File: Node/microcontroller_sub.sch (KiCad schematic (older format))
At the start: 53 parts, among them SW1701 SW_Push, U1701 IC_MICROCHIP_SAMD21G18A-A, Y2301 32.768kHz, Y2302 25MHz

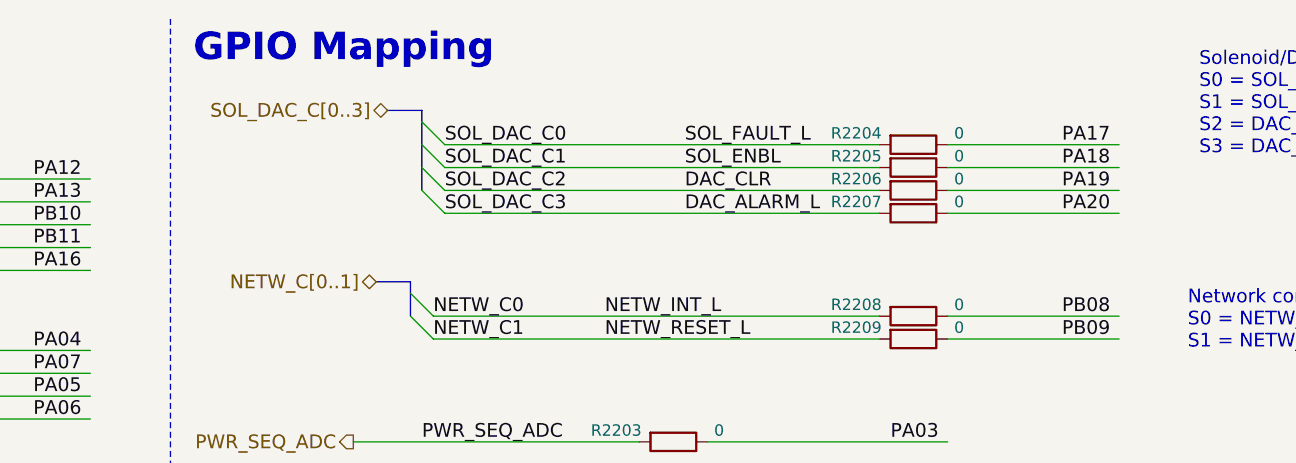
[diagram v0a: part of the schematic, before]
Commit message: All layout done. Added PU to the ADC mux. Assigned SAMD pins to the DAC power sequencer I/O. Cleaned up the power layer. Time for DRC, cleaning, minute tweaks, and documentation/BOM
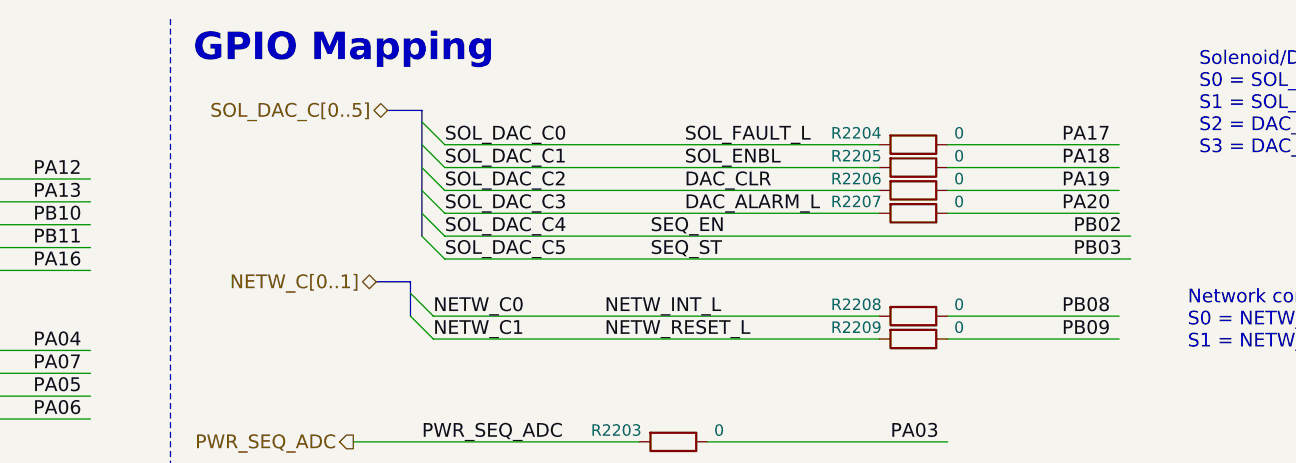
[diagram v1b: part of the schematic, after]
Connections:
- net labels added: SEQ_EN, SEQ_ST, SOL_DAC_C4, SOL_DAC_C5, SOL_DAC_C[0..5]
- net labels removed: SOL_DAC_C[0..3]
- wire segments 161 -> 163
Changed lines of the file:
@@
 I2C Capable Pins:\nSERCOM4: 21+22\nSERCOM3: 25+26\nSERCOM5: 31+32\nSERCOM2: 13+14\n
 $Comp
-L GND #PWR2213
+L GND #PWR2214
 U 1 1 59E6B342
 P 6750 10150
-F 0 "#PWR2213" H 6750 9900 50  0001 C CNN
+F 0 "#PWR2214" H 6750 9900 50  0001 C CNN
 F 1 "GND" H 6750 10000 50  0000 C CNN
 F 2 "" H 6750 10150 50  0000 C CNN
@@
 $EndComp
 $Comp
-L GND #PWR2205
+L GND #PWR2207
 U 1 1 59E72263
 P 1250 4350
-F 0 "#PWR2205" H 1250 4100 50  0001 C CNN
+F 0 "#PWR2207" H 1250 4100 50  0001 C CNN
 F 1 "GND" H 1250 4200 50  0000 C CNN
 F 2 "" H 1250 4350 50  0000 C CNN
@@
 VDDCORE_1V2
 $Comp
-L GND #PWR2211
+L GND #PWR2204
 U 1 1 5A0AA08F
 P 4500 2100
-F 0 "#PWR2211" H 4500 1850 50  0001 C CNN
+F 0 "#PWR2204" H 4500 1850 50  0001 C CNN
 F 1 "GND" H 4500 1950 50  0000 C CNN
 F 2 "" H 4500 2100 50  0001 C CNN
@@
 RESET_L
 $Comp
-L GND #PWR2208
+L GND #PWR2206
 U 1 1 5A0AC21B
 P 2100 4200
-F 0 "#PWR2208" H 2100 3950 50  0001 C CNN
+F 0 "#PWR2206" H 2100 3950 50  0001 C CNN
 F 1 "GND" H 2100 4050 50  0000 C CNN
 F 2 "" H 2100 4200 50  0000 C CNN
@@
 GPIO Mapping
 Text HLabel 11150 900  0    60   BiDi ~ 0
-SOL_DAC_C[0..3]
+SOL_DAC_C[0..5]
 Entry Wire Line
 	11300 950  11400 1050
@@
 $EndComp
 $Comp
-L GND #PWR2210
+L GND #PWR2203
 U 1 1 5A13F166
 P 2800 2000
-F 0 "#PWR2210" H 2800 1750 50  0001 C CNN
+F 0 "#PWR2203" H 2800 1750 50  0001 C CNN
 F 1 "GND" H 2800 1850 50  0000 C CNN
 F 2 "" H 2800 2000 50  0001 C CNN
@@
 $EndComp
 $Comp
-L +3V3 #PWR2202
+L +3V3 #PWR2201
 U 1 1 5A13F196
 P 850 1200
-F 0 "#PWR2202" H 850 1050 50  0001 C CNN
+F 0 "#PWR2201" H 850 1050 50  0001 C CNN
 F 1 "+3V3" H 850 1340 50  0000 C CNN
 F 2 "" H 850 1200 50  0001 C CNN
@@
 $EndComp
 $Comp
-L GND #PWR2203
+L GND #PWR2202
 U 1 1 5A1411D0
 P 850 2000
-F 0 "#PWR2203" H 850 1750 50  0001 C CNN
+F 0 "#PWR2202" H 850 1750 50  0001 C CNN
 F 1 "GND" H 850 1850 50  0000 C CNN
 F 2 "" H 850 2000 50  0001 C CNN
@@
 $EndComp
 $Comp
-L +3V3 #PWR2209
+L +3V3 #PWR2205
 U 1 1 5A1416C8
 P 2700 2800
-F 0 "#PWR2209" H 2700 2650 50  0001 C CNN
+F 0 "#PWR2205" H 2700 2650 50  0001 C CNN
 F 1 "+3V3" H 2700 2940 50  0000 C CNN
 F 2 "" H 2700 2800 50  0001 C CNN
@@
 3V3A_SAMD
 $Comp
-L +3V3 #PWR2212
+L +3V3 #PWR2209
 U 1 1 5A142050
 P 6450 6200
-F 0 "#PWR2212" H 6450 6050 50  0001 C CNN
+F 0 "#PWR2209" H 6450 6050 50  0001 C CNN
 F 1 "+3V3" H 6450 6340 50  0000 C CNN
 F 2 "" H 6450 6200 50  0001 C CNN
@@
 $EndComp
 $Comp
-L +3V3 #PWR2214
+L +3V3 #PWR2208
 U 1 1 5A0D576C
 P 7700 4650
-F 0 "#PWR2214" H 7700 4500 50  0001 C CNN
+F 0 "#PWR2208" H 7700 4500 50  0001 C CNN
 F 1 "+3V3" H 7700 4790 50  0000 C CNN
 F 2 "" H 7700 4650 50  0001 C CNN
@@
 $EndComp
 $Comp
-L GND #PWR2201
+L GND #PWR2210
 U 1 1 5A0DF272
 P 800 6600
-F 0 "#PWR2201" H 800 6350 50  0001 C CNN
+F 0 "#PWR2210" H 800 6350 50  0001 C CNN
 F 1 "GND" H 800 6450 50  0000 C CNN
 F 2 "" H 800 6600 50  0000 C CNN
@@
 $EndComp
 $Comp
-L GND #PWR2206
+L GND #PWR2211
 U 1 1 5A0DF2F9
 P 1600 6600
-F 0 "#PWR2206" H 1600 6350 50  0001 C CNN
+F 0 "#PWR2211" H 1600 6350 50  0001 C CNN
 F 1 "GND" H 1600 6450 50  0000 C CNN
 F 2 "" H 1600 6600 50  0000 C CNN
@@
 $EndComp
 $Comp
-L GND #PWR2204
+L GND #PWR2212
 U 1 1 5A0E3348
 P 850 8900
-F 0 "#PWR2204" H 850 8650 50  0001 C CNN
+F 0 "#PWR2212" H 850 8650 50  0001 C CNN
 F 1 "GND" H 850 8750 50  0000 C CNN
 F 2 "" H 850 8900 50  0000 C CNN
@@
 $EndComp
 $Comp
-L GND #PWR2207
+L GND #PWR2213
 U 1 1 5A0E334F
 P 1650 8900
-F 0 "#PWR2207" H 1650 8650 50  0001 C CNN
+F 0 "#PWR2213" H 1650 8650 50  0001 C CNN
 F 1 "GND" H 1650 8750 50  0000 C CNN
 F 2 "" H 1650 8900 50  0000 C CNN
@@
 	500  4750 3650 4750
 Wire Bus Line
-	11300 900  11300 1250
+	11300 900  11300 1450
 Wire Wire Line
 	11400 1050 13300 1050
@@
 Text Label 13350 2350 0    60   ~ 0
 PA03
+Text Label 11400 1450 0    60   ~ 0
+SOL_DAC_C4
+Text Label 11400 1550 0    60   ~ 0
+SOL_DAC_C5
+Entry Wire Line
+	11300 1350 11400 1450
+Entry Wire Line
+	11300 1450 11400 1550
+Wire Wire Line
+	11400 1450 14400 1450
+Wire Wire Line
+	11400 1550 14400 1550
+Text Label 12300 1450 0    60   ~ 0
+SEQ_EN
+Text Label 12300 1550 0    60   ~ 0
+SEQ_ST
+Text Label 14150 1450 0    60   ~ 0
+PB02
+Text Label 14150 1550 0    60   ~ 0
+PB03
 $EndSCHEMATC

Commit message: Generated BOM, filled out part numbers for precision resistors and headers.
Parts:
- SW1701: MFG. P/N (none) -> PTS645SM43SMTR92 LFS; Manufacturer (none) -> C&K; Vendor (none) -> DigiKey; Vendor P/N (none) -> CKN9112CT-ND
- U1701: MFG. P/N (none) -> ATSAMD21G18A-AUT; Manufacturer (none) -> Microchip Technology; Vendor (none) -> DigiKey; Vendor P/N (none) -> ATSAMD21G18A-AUTCT-ND
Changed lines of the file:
@@
 EESchema Schematic File Version 2
 LIBS:hyper_capstone
+LIBS:Connector
 LIBS:node-cache
 EELAYER 25 0
@@
 I2C Capable Pins:\nSERCOM4: 21+22\nSERCOM3: 25+26\nSERCOM5: 31+32\nSERCOM2: 13+14\n
 $Comp
-L GND #PWR2214
+L GND #PWR0218
 U 1 1 59E6B342
 P 6750 10150
-F 0 "#PWR2214" H 6750 9900 50  0001 C CNN
+F 0 "#PWR0218" H 6750 9900 50  0001 C CNN
 F 1 "GND" H 6750 10000 50  0000 C CNN
 F 2 "" H 6750 10150 50  0000 C CNN
@@
 $EndComp
 $Comp
-L GND #PWR2207
+L GND #PWR0219
 U 1 1 59E72263
 P 1250 4350
-F 0 "#PWR2207" H 1250 4100 50  0001 C CNN
+F 0 "#PWR0219" H 1250 4100 50  0001 C CNN
 F 1 "GND" H 1250 4200 50  0000 C CNN
 F 2 "" H 1250 4350 50  0000 C CNN
@@
 VDDCORE_1V2
 $Comp
-L GND #PWR2204
+L GND #PWR0220
 U 1 1 5A0AA08F
 P 4500 2100
-F 0 "#PWR2204" H 4500 1850 50  0001 C CNN
+F 0 "#PWR0220" H 4500 1850 50  0001 C CNN
 F 1 "GND" H 4500 1950 50  0000 C CNN
 F 2 "" H 4500 2100 50  0001 C CNN
@@
 RESET_L
 $Comp
-L GND #PWR2206
+L GND #PWR0221
 U 1 1 5A0AC21B
 P 2100 4200
-F 0 "#PWR2206" H 2100 3950 50  0001 C CNN
+F 0 "#PWR0221" H 2100 3950 50  0001 C CNN
 F 1 "GND" H 2100 4050 50  0000 C CNN
 F 2 "" H 2100 4200 50  0000 C CNN
@@
 $EndComp
 $Comp
-L GND #PWR2203
+L GND #PWR0222
 U 1 1 5A13F166
 P 2800 2000
-F 0 "#PWR2203" H 2800 1750 50  0001 C CNN
+F 0 "#PWR0222" H 2800 1750 50  0001 C CNN
 F 1 "GND" H 2800 1850 50  0000 C CNN
 F 2 "" H 2800 2000 50  0001 C CNN
@@
 $EndComp
 $Comp
-L +3V3 #PWR2201
+L +3V3 #PWR0223
 U 1 1 5A13F196
 P 850 1200
-F 0 "#PWR2201" H 850 1050 50  0001 C CNN
+F 0 "#PWR0223" H 850 1050 50  0001 C CNN
 F 1 "+3V3" H 850 1340 50  0000 C CNN
 F 2 "" H 850 1200 50  0001 C CNN
@@
 $EndComp
 $Comp
-L GND #PWR2202
+L GND #PWR0224
 U 1 1 5A1411D0
 P 850 2000
-F 0 "#PWR2202" H 850 1750 50  0001 C CNN
+F 0 "#PWR0224" H 850 1750 50  0001 C CNN
 F 1 "GND" H 850 1850 50  0000 C CNN
 F 2 "" H 850 2000 50  0001 C CNN
@@
 $EndComp
 $Comp
-L +3V3 #PWR2205
+L +3V3 #PWR0225
 U 1 1 5A1416C8
 P 2700 2800
-F 0 "#PWR2205" H 2700 2650 50  0001 C CNN
+F 0 "#PWR0225" H 2700 2650 50  0001 C CNN
 F 1 "+3V3" H 2700 2940 50  0000 C CNN
 F 2 "" H 2700 2800 50  0001 C CNN
@@
 3V3A_SAMD
 $Comp
-L +3V3 #PWR2209
+L +3V3 #PWR0226
 U 1 1 5A142050
 P 6450 6200
-F 0 "#PWR2209" H 6450 6050 50  0001 C CNN
+F 0 "#PWR0226" H 6450 6050 50  0001 C CNN
 F 1 "+3V3" H 6450 6340 50  0000 C CNN
 F 2 "" H 6450 6200 50  0001 C CNN
@@
 $EndComp
 $Comp
-L +3V3 #PWR2208
+L +3V3 #PWR0227
 U 1 1 5A0D576C
 P 7700 4650
-F 0 "#PWR2208" H 7700 4500 50  0001 C CNN
+F 0 "#PWR0227" H 7700 4500 50  0001 C CNN
 F 1 "+3V3" H 7700 4790 50  0000 C CNN
 F 2 "" H 7700 4650 50  0001 C CNN
@@
 $EndComp
 $Comp
-L GND #PWR2210
+L GND #PWR0228
 U 1 1 5A0DF272
 P 800 6600
-F 0 "#PWR2210" H 800 6350 50  0001 C CNN
+F 0 "#PWR0228" H 800 6350 50  0001 C CNN
 F 1 "GND" H 800 6450 50  0000 C CNN
 F 2 "" H 800 6600 50  0000 C CNN
@@
 $EndComp
 $Comp
-L GND #PWR2211
+L GND #PWR0229
 U 1 1 5A0DF2F9
 P 1600 6600
-F 0 "#PWR2211" H 1600 6350 50  0001 C CNN
+F 0 "#PWR0229" H 1600 6350 50  0001 C CNN
 F 1 "GND" H 1600 6450 50  0000 C CNN
 F 2 "" H 1600 6600 50  0000 C CNN
@@
 $EndComp
 $Comp
-L GND #PWR2212
+L GND #PWR0230
 U 1 1 5A0E3348
 P 850 8900
-F 0 "#PWR2212" H 850 8650 50  0001 C CNN
+F 0 "#PWR0230" H 850 8650 50  0001 C CNN
 F 1 "GND" H 850 8750 50  0000 C CNN
 F 2 "" H 850 8900 50  0000 C CNN
@@
 $EndComp
 $Comp
-L GND #PWR2213
+L GND #PWR0231
 U 1 1 5A0E334F
 P 1650 8900
-F 0 "#PWR2213" H 1650 8650 50  0001 C CNN
+F 0 "#PWR0231" H 1650 8650 50  0001 C CNN
 F 1 "GND" H 1650 8750 50  0000 C CNN
 F 2 "" H 1650 8900 50  0000 C CNN
@@
 F 2 "Housings_QFP:TQFP-48_7x7mm_Pitch0.5mm" H 7050 7050 50  0001 C CIN
 F 3 "" H 7050 8450 50  0000 C CNN
+F 4 "Microchip Technology" H 7050 8200 60  0001 C CNN "Manufacturer"
+F 5 "ATSAMD21G18A-AUT" H 7050 8200 60  0001 C CNN "MFG. P/N"
+F 6 "DigiKey" H 7050 8200 60  0001 C CNN "Vendor"
+F 7 "ATSAMD21G18A-AUTCT-ND" H 7050 8200 60  0001 C CNN "Vendor P/N"
 	1    7050 8200
 	1    0    0    -1
@@
 F 2 "hyperCustom:C&K_switch_PTS645SM43SMTR92" H 1250 4150 50  0001 C CNN
 F 3 "" H 1250 4150 50  0001 C CNN
+F 4 "C&K" H 1250 3950 60  0001 C CNN "Manufacturer"
+F 5 "PTS645SM43SMTR92 LFS" H 1250 3950 60  0001 C CNN "MFG. P/N"
+F 6 "DigiKey" H 1250 3950 60  0001 C CNN "Vendor"
+F 7 "CKN9112CT-ND" H 1250 3950 60  0001 C CNN "Vendor P/N"
 	1    1250 3950
 	0    -1   -1   0

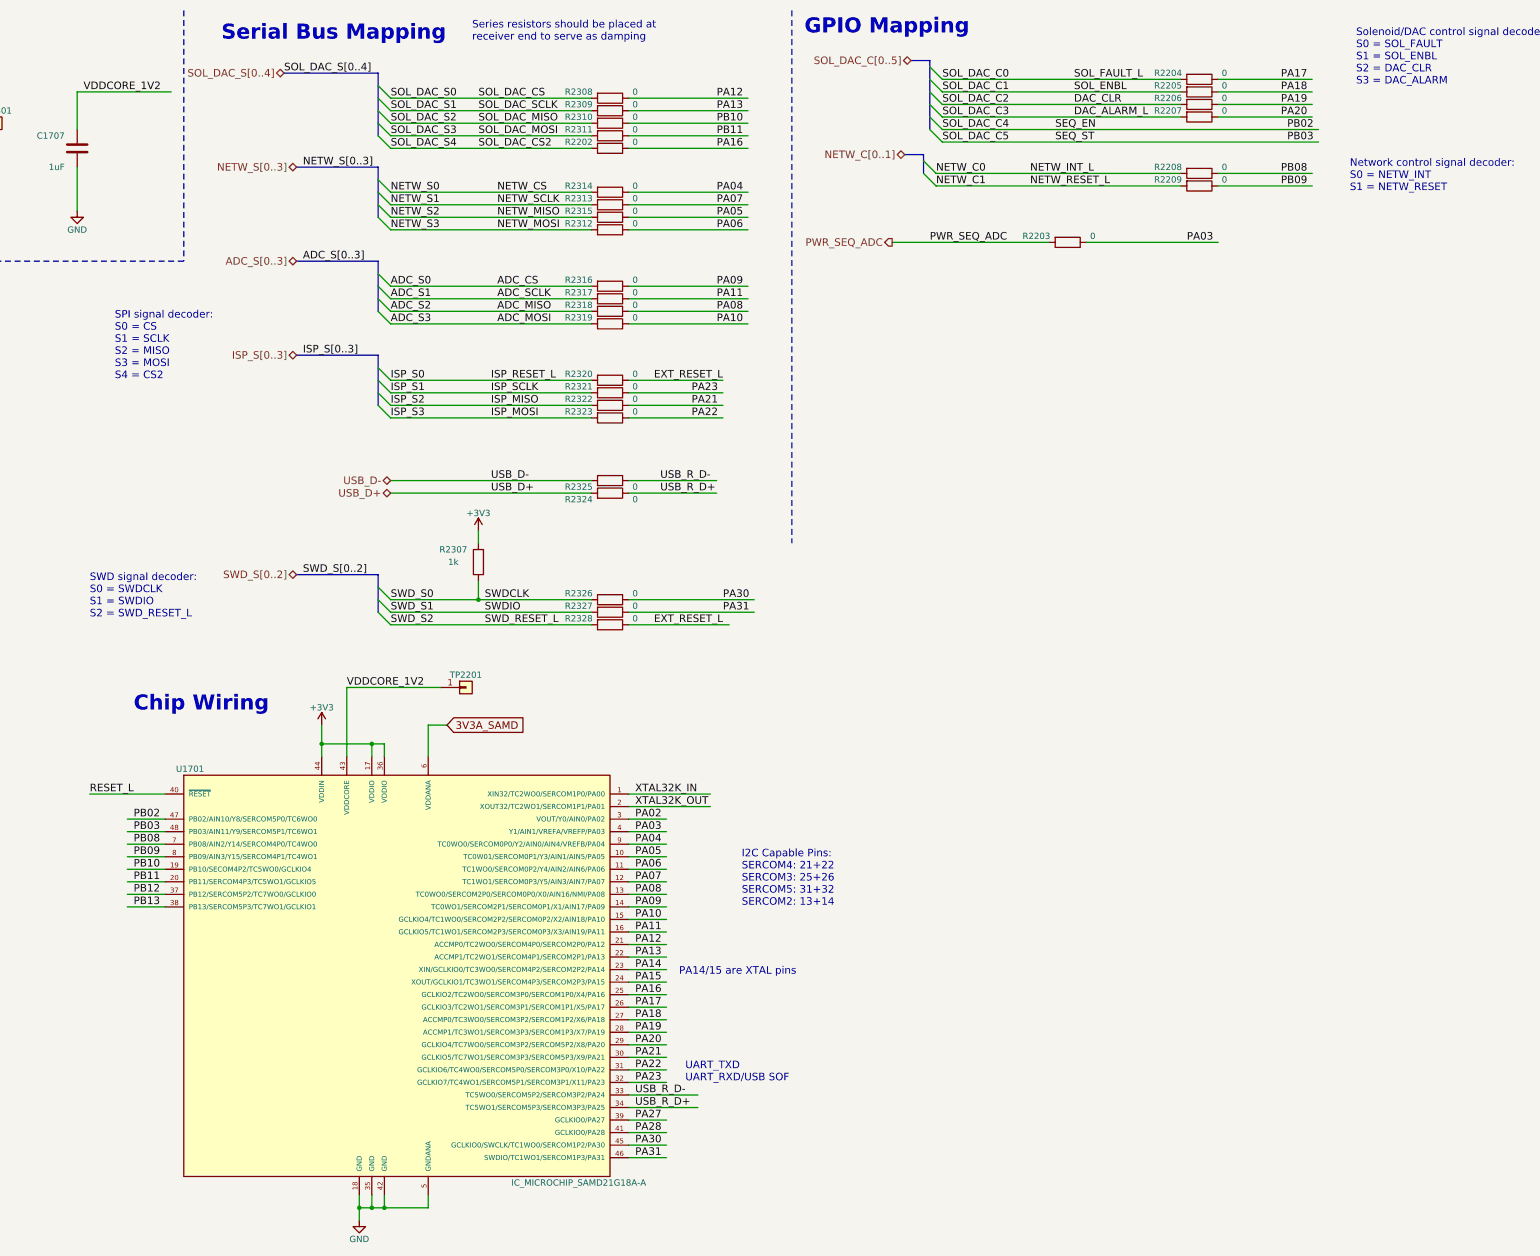
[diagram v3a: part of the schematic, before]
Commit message: fixed and routed driver spi issue
Added new rx/tx bus for solenoid driver. Routed it too. Nice.
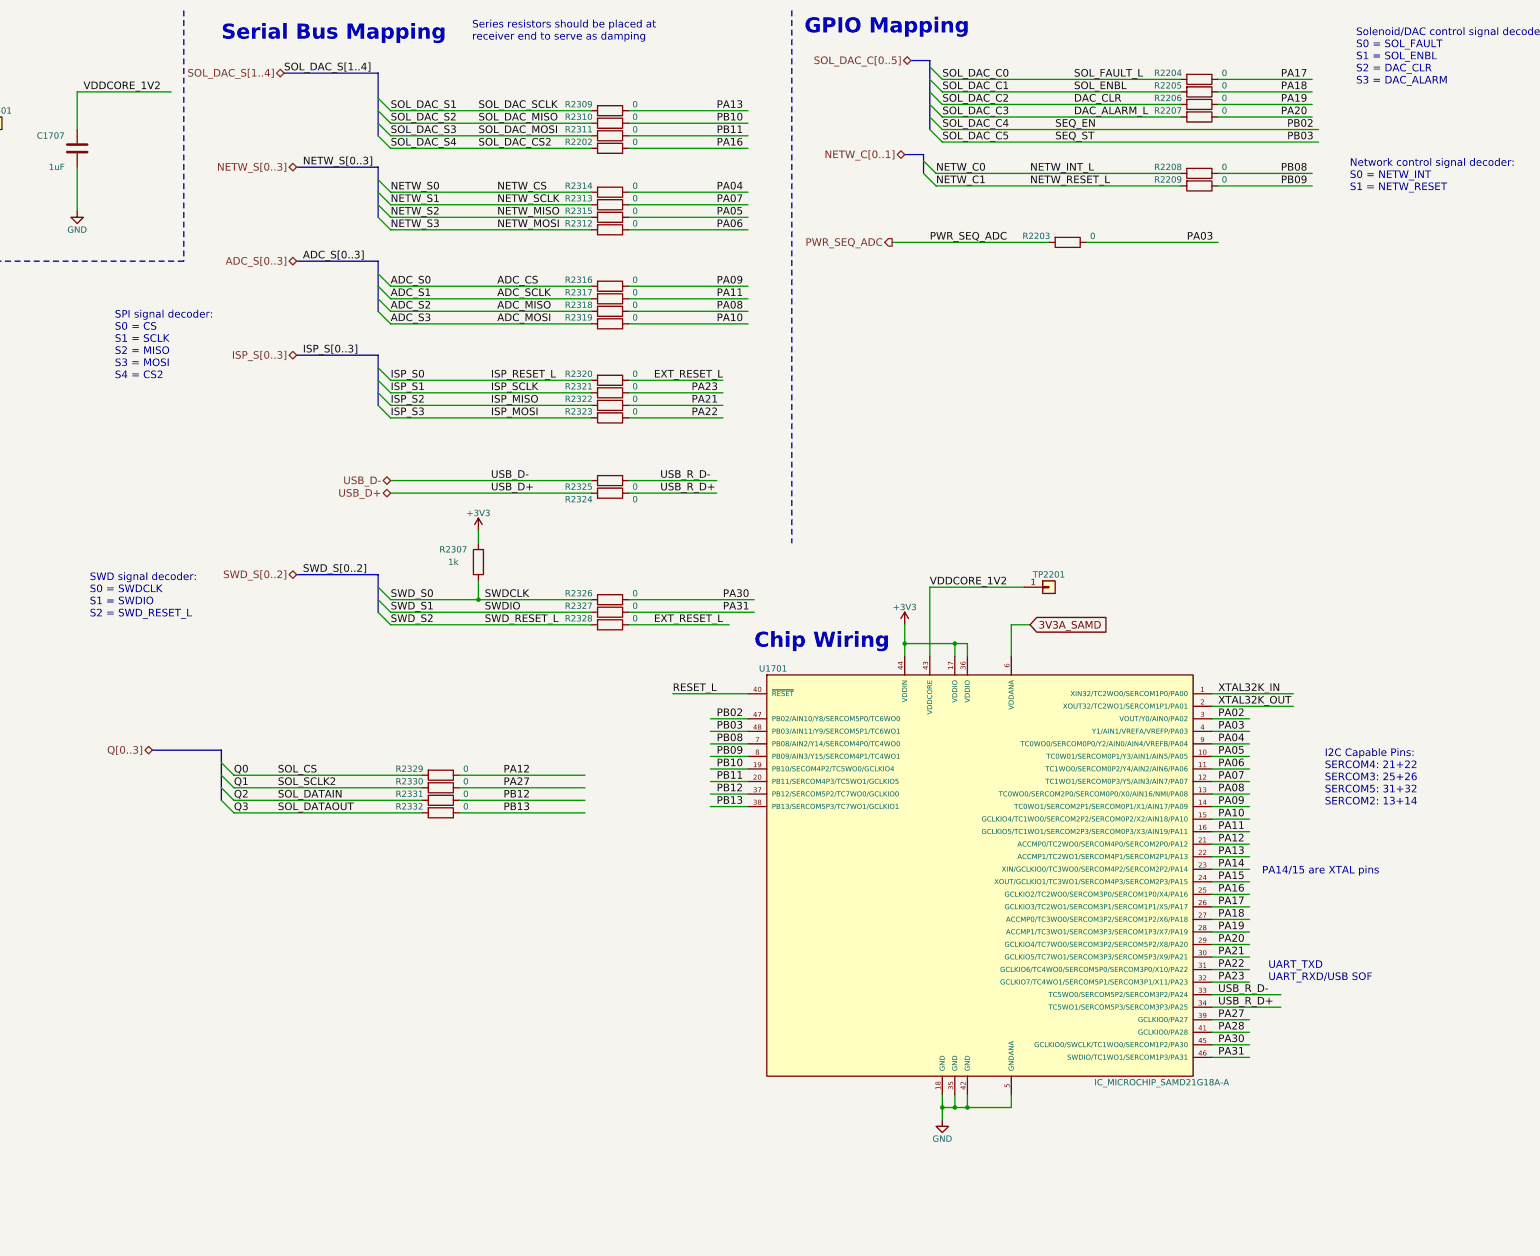
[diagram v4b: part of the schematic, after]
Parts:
- removed R2308: 0, Resistors_SMD:R_0805_HandSoldering, symbol R
- added R2329, R2330, R2331, R2332: 0, Resistors_SMD:R_0805_HandSoldering, symbol R
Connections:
- net labels added: Q0, Q1, Q2, Q3, Q[0..3], SOL_CS, SOL_DAC_S[1..4], SOL_DATAIN, SOL_DATAOUT, SOL_SCLK2
- net labels removed: SOL_DAC_CS, SOL_DAC_S0, SOL_DAC_S[0..4]
- wire segments 163 -> 169
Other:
- moved on the sheet: TP2201, U1701

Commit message: Ghost train
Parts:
- C1702, C1707, C2301, C2302, C2303, C2304, C2305, C2306, C2307, C2308, C2309, C2310: symbol C -> node-rescue:C
- L2301: symbol Ferrite_Bead_Small -> node-rescue:Ferrite_Bead_Small
- R1701, R1702, R2202, R2203, R2204, R2205, R2206, R2207, R2208, R2209, R2301, R2302, R2307, R2309, R2310, R2311, R2312, R2313, R2314, R2315, R2316, R2317, R2318, R2319, R2320, R2321, R2322, R2323, R2324, R2325, R2326, R2327, R2328, R2329, R2330, R2331, R2332: symbol R -> node-rescue:R
- SW1701: symbol SW_Push -> node-rescue:SW_Push
- TP2201, TP2301: symbol Conn_01x01 -> node-rescue:Conn_01x01
- U1701: symbol IC_MICROCHIP_SAMD21G18A-A -> hyper_capstone:IC_MICROCHIP_SAMD21G18A-A
- Y2301, Y2302: symbol Crystal -> node-rescue:Crystal
